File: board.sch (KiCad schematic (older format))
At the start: 13 parts, among them J1 chip_inst_mem_o, J10 chip_data_mem_o_1, J11 base, J12 power, J2 chip_data_mem_o_1, J3 data_mem_i, J4 chip_data_mem_o_1, J5 data_mem_i, J6 chip_data_mem_o_3, J7 inst_mem_i, J8 inst_mem_i, J9 chip_data_mem_o_1, U1 BERYL-MBLite

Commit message: Change headers to SMD and add decoupling capacitors
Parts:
- removed J10, J4, J9: chip_data_mem_o_1, Connector_PinSocket_2.54mm:PinSocket_1x16_P2.54mm_Vertical, symbol Connector:Conn_01x16_Female
- removed J5: data_mem_i, Connector_PinSocket_2.54mm:PinSocket_1x17_P2.54mm_Vertical, symbol Connector:Conn_01x17_Female
- removed J6: chip_data_mem_o_3, Connector_PinSocket_2.54mm:PinSocket_1x06_P2.54mm_Vertical, symbol Connector:Conn_01x06_Female
- removed J8: inst_mem_i, Connector_PinSocket_2.54mm:PinSocket_1x16_P2.54mm_Vertical, symbol Connector:Conn_01x16_Female
- added C1, C10, C11, C12, C13, C14, C15, C16, C17, C18, C19, C2, C20, C21, C22, C23, C24, C25, C3, C4, C5, C6, C7, C8, C9: 100n, Capacitor_SMD:C_0805_2012Metric_Pad1.15x1.40mm_HandSolder, symbol Device:C_Small
- added H1, H2, H3, H4: MountingHole, MountingHole:MountingHole_2.5mm, symbol Mechanical:MountingHole
- added J4: chip_data_mem_o_1, Connector_PinSocket_2.54mm:PinSocket_2x18_P2.54mm_Vertical_SMD, symbol Connector:Conn_01x35_Female
- J1: footprint Connector_PinSocket_2.54mm:PinSocket_1x17_P2.54mm_Vertical -> Connector_PinSocket_2.54mm:PinSocket_2x09_P2.54mm_Vertical_SMD
- J11: footprint Connector_PinSocket_2.54mm:PinSocket_1x05_P2.54mm_Vertical -> Connector_PinSocket_2.54mm:PinSocket_2x03_P2.54mm_Vertical_SMD; symbol Connector:Conn_01x05_Female -> Connector:Conn_01x06_Female
- J12: footprint Connector_PinSocket_2.54mm:PinSocket_1x08_P2.54mm_Vertical -> Connector_PinSocket_2.54mm:PinSocket_2x04_P2.54mm_Vertical_SMD
- J2: footprint Connector_PinSocket_2.54mm:PinSocket_1x16_P2.54mm_Vertical -> Connector_PinSocket_2.54mm:PinSocket_2x18_P2.54mm_Vertical_SMD; symbol Connector:Conn_01x16_Female -> Connector:Conn_01x35_Female
- J3: footprint Connector_PinSocket_2.54mm:PinSocket_1x16_P2.54mm_Vertical -> Connector_PinSocket_2.54mm:PinSocket_2x17_P2.54mm_Vertical_SMD; symbol Connector:Conn_01x16_Female -> Connector:Conn_01x34_Female
- J7: footprint Connector_PinSocket_2.54mm:PinSocket_1x16_P2.54mm_Vertical -> Connector_PinSocket_2.54mm:PinSocket_2x16_P2.54mm_Vertical_SMD; symbol Connector:Conn_01x16_Female -> Connector:Conn_01x32_Female
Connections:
- net +1V8: now also C11.1, C12.1, C13.1, C14.1, C15.1, C16.1, C17.1, C18.1, C19.1, C20.1, C21.1, C22.1, C23.1, C24.1, C25.1
- net +3V3: now also C1.1, C10.1, C2.1, C3.1, C4.1, C5.1, C6.1, C7.1, C8.1, C9.1
- net GND: now also J11.6 (Pin_6), C1.2, C10.2, C11.2, C12.2, C13.2, C14.2, C15.2, C16.2, C17.2, C18.2, C19.2, C2.2, C20.2, C21.2, C22.2, C23.2, C24.2, C25.2, C3.2, C4.2, C5.2, C6.2, C7.2, C8.2, C9.2
- net at U1.153 (data_mem_i_32): now also J3.33 (Pin_33)
- net at U1.154 (data_mem_i_31): now also J3.32 (Pin_32)
- net at U1.155 (data_mem_i_30): now also J3.31 (Pin_31)
- net at U1.156 (data_mem_i_29): now also J3.30 (Pin_30)
- net at U1.157 (data_mem_i_28): now also J3.29 (Pin_29)
- net at U1.158 (data_mem_i_27): now also J3.28 (Pin_28)
- net at U1.159 (data_mem_i_26): now also J3.27 (Pin_27)
- net at U1.160 (data_mem_i_25): now also J3.26 (Pin_26)
- net at U1.163 (data_mem_i_24): now also J3.25 (Pin_25)
- net at U1.164 (data_mem_i_23): now also J3.24 (Pin_24)
- net at U1.165 (data_mem_i_22): now also J3.23 (Pin_23)
- net at U1.166 (data_mem_i_21): now also J3.22 (Pin_22)
- net at U1.167 (data_mem_i_20): now also J3.21 (Pin_21)
- net at U1.168 (data_mem_i_19): now also J3.20 (Pin_20)
- net at U1.169 (data_mem_i_18): now also J3.19 (Pin_19)
- net at U1.170 (data_mem_i_17): now also J3.18 (Pin_18)
- net at U1.171 (data_mem_i_16): now also J3.17 (Pin_17)
- net at U1.1 (inst_mem_i_22): now also J7.10 (Pin_10)
- net at U1.10 (inst_mem_i_15): now also J7.17 (Pin_17); no longer J7.1 (Pin_1)
- net at U1.11 (inst_mem_i_14): now also J7.18 (Pin_18); no longer J7.2 (Pin_2)
- net at U1.12 (inst_mem_i_13): now also J7.19 (Pin_19); no longer J7.3 (Pin_3)
- net at U1.13 (inst_mem_i_12): now also J7.20 (Pin_20); no longer J7.4 (Pin_4)
- net at U1.14 (inst_mem_i_11): now also J7.21 (Pin_21); no longer J7.5 (Pin_5)
- net at U1.15 (inst_mem_i_10): now also J7.22 (Pin_22); no longer J7.6 (Pin_6)
- net at U1.18 (inst_mem_i_9): now also J7.23 (Pin_23); no longer J7.7 (Pin_7)
- net at U1.19 (inst_mem_i_8): now also J7.24 (Pin_24); no longer J7.8 (Pin_8)
- net at U1.192 (inst_mem_i_31): now also J7.1 (Pin_1)
- net at U1.193 (inst_mem_i_30): now also J7.2 (Pin_2)
- net at U1.2 (inst_mem_i_21): now also J7.11 (Pin_11)
- net at U1.20 (inst_mem_i_7): now also J7.25 (Pin_25); no longer J7.9 (Pin_9)
- net at U1.202 (inst_mem_i_29): now also J7.3 (Pin_3)
- net at U1.203 (inst_mem_i_28): now also J7.4 (Pin_4)
- net at U1.204 (inst_mem_i_27): now also J7.5 (Pin_5)
- net at U1.205 (inst_mem_i_26): now also J7.6 (Pin_6)
- net at U1.206 (inst_mem_i_25): now also J7.7 (Pin_7)
- net at U1.207 (inst_mem_i_24): now also J7.8 (Pin_8)
- net at U1.208 (inst_mem_i_23): now also J7.9 (Pin_9)
- net at U1.21 (inst_mem_i_6): now also J7.26 (Pin_26); no longer J7.10 (Pin_10)
- net at U1.22 (inst_mem_i_5): now also J7.27 (Pin_27); no longer J7.11 (Pin_11)
- net at U1.23 (inst_mem_i_4): now also J7.28 (Pin_28); no longer J7.12 (Pin_12)
- net at U1.24 (inst_mem_i_3): now also J7.29 (Pin_29); no longer J7.13 (Pin_13)
- net at U1.27 (inst_mem_i_2): now also J7.30 (Pin_30); no longer J7.14 (Pin_14)
- net at U1.28 (inst_mem_i_1): now also J7.31 (Pin_31); no longer J7.15 (Pin_15)
- net at U1.29 (inst_mem_i_0): now also J7.32 (Pin_32); no longer J7.16 (Pin_16)
- net at U1.3 (inst_mem_i_20): now also J7.12 (Pin_12)
- net at U1.4 (inst_mem_i_19): now also J7.13 (Pin_13)
- net at U1.5 (inst_mem_i_18): now also J7.14 (Pin_14)
- net at U1.6 (inst_mem_i_17): now also J7.15 (Pin_15)
- net at U1.7 (inst_mem_i_16): now also J7.16 (Pin_16)
- net at U1.100 (chip_data_mem_o_20): now also J2.21 (Pin_21)
- net at U1.101 (chip_data_mem_o_19): now also J2.20 (Pin_20)
- net at U1.102 (chip_data_mem_o_18): now also J2.19 (Pin_19)
- net at U1.103 (chip_data_mem_o_17): now also J2.18 (Pin_18)
- net at U1.104 (chip_data_mem_o_16): now also J2.17 (Pin_17)
- net at U1.107 (chip_data_mem_o_36): now also J4.2 (Pin_2)
- net at U1.108 (chip_data_mem_o_37): now also J4.3 (Pin_3)
- net at U1.109 (chip_data_mem_o_38): now also J4.4 (Pin_4)
- net at U1.110 (chip_data_mem_o_39): now also J4.5 (Pin_5)
- net at U1.111 (chip_data_mem_o_40): now also J4.6 (Pin_6)
- net at U1.112 (chip_data_mem_o_41): now also J4.7 (Pin_7)
- net at U1.113 (chip_data_mem_o_42): now also J4.8 (Pin_8)
- net at U1.114 (chip_data_mem_o_43): now also J4.9 (Pin_9)
- net at U1.115 (chip_data_mem_o_44): now also J4.10 (Pin_10)
- net at U1.118 (chip_data_mem_o_45): now also J4.11 (Pin_11)
- net at U1.119 (chip_data_mem_o_46): now also J4.12 (Pin_12)
- net at U1.122 (chip_data_mem_o_47): now also J4.13 (Pin_13)
- net at U1.123 (chip_data_mem_o_48): now also J4.14 (Pin_14)
- net at U1.124 (chip_data_mem_o_49): now also J4.15 (Pin_15)
- net at U1.125 (chip_data_mem_o_50): now also J4.16 (Pin_16)
- net at U1.126 (chip_data_mem_o_51): now also J4.17 (Pin_17)
- net at U1.127 (chip_data_mem_o_52): now also J4.18 (Pin_18)
- net at U1.128 (chip_data_mem_o_53): now also J4.19 (Pin_19)
- net at U1.129 (chip_data_mem_o_54): now also J4.20 (Pin_20)
- net at U1.130 (chip_data_mem_o_55): now also J4.21 (Pin_21)
- net at U1.131 (chip_data_mem_o_56): now also J4.22 (Pin_22)
- net at U1.132 (chip_data_mem_o_57): now also J4.23 (Pin_23)
- net at U1.133 (chip_data_mem_o_58): now also J4.24 (Pin_24)
- net at U1.136 (chip_data_mem_o_59): now also J4.25 (Pin_25)
- net at U1.139 (chip_data_mem_o_60): now also J4.26 (Pin_26)
- net at U1.140 (chip_data_mem_o_61): now also J4.27 (Pin_27)
- net at U1.141 (chip_data_mem_o_62): now also J4.28 (Pin_28)
- net at U1.142 (chip_data_mem_o_63): now also J4.29 (Pin_29)
- net at U1.143 (chip_data_mem_o_64): now also J4.30 (Pin_30)
- net at U1.144 (chip_data_mem_o_65): now also J4.31 (Pin_31)
- net at U1.145 (chip_data_mem_o_66): now also J4.32 (Pin_32)
- net at U1.146 (chip_data_mem_o_67): now also J4.33 (Pin_33)
- net at U1.147 (chip_data_mem_o_68): now also J4.34 (Pin_34)
- net at U1.148 (chip_data_mem_o_69): now also J4.35 (Pin_35)
- net at U1.79 (chip_data_mem_o_35): now also J4.1 (Pin_1)
- net at U1.80 (chip_data_mem_o_34): now also J2.35 (Pin_35)
- net at U1.81 (chip_data_mem_o_33): now also J2.34 (Pin_34)
- net at U1.82 (chip_data_mem_o_32): now also J2.33 (Pin_33)
- net at U1.83 (chip_data_mem_o_31): now also J2.32 (Pin_32)
- net at U1.84 (chip_data_mem_o_30): now also J2.31 (Pin_31)
- net at U1.85 (chip_data_mem_o_29): now also J2.30 (Pin_30)
- net at U1.88 (chip_data_mem_o_28): now also J2.29 (Pin_29)
- net at U1.89 (chip_data_mem_o_27): now also J2.28 (Pin_28)
- net at U1.90 (chip_data_mem_o_26): now also J2.27 (Pin_27)
- net at U1.93 (chip_data_mem_o_25): now also J2.26 (Pin_26)
- net at U1.94 (chip_data_mem_o_24): now also J2.25 (Pin_25)
- net at U1.95 (chip_data_mem_o_23): now also J2.24 (Pin_24)
- net at U1.96 (chip_data_mem_o_22): now also J2.23 (Pin_23)
- net at U1.99 (chip_data_mem_o_21): now also J2.22 (Pin_22)
- no-connect marks 0 -> 1
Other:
- moved on the sheet: J12, U1F

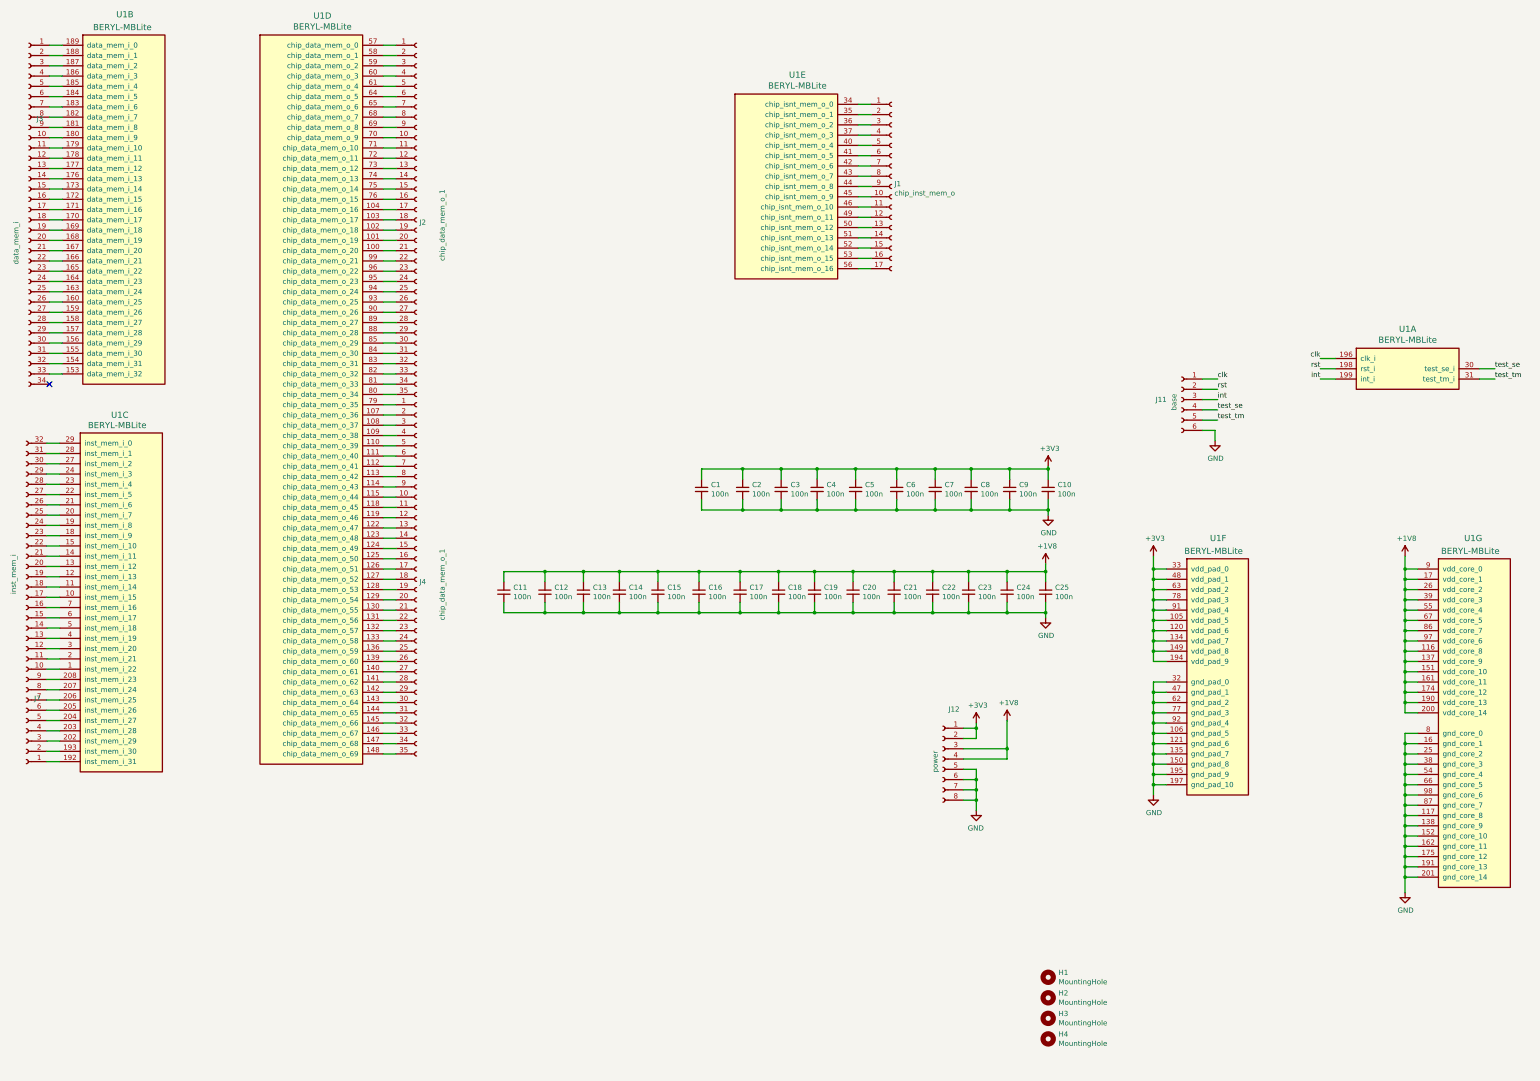
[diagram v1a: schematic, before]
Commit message: Improve capacitors placement
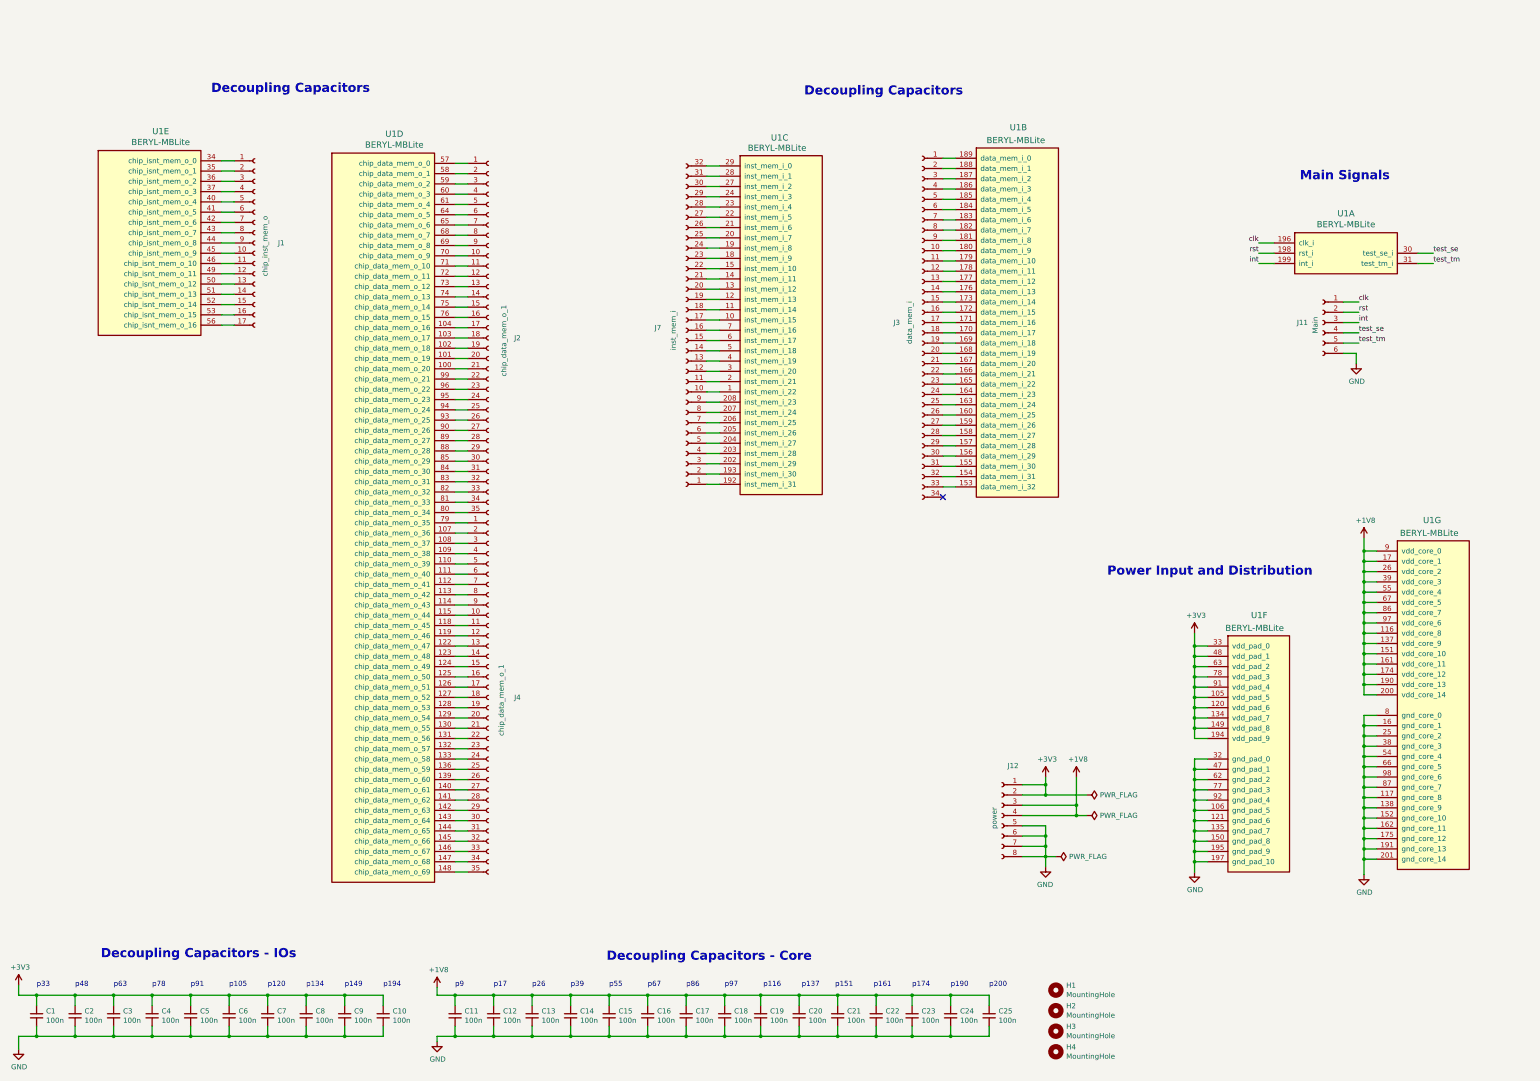
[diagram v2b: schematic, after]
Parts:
- J11: value base -> Main
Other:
- note added: "Decoupling Capacitors"
- note added: "Decoupling Capacitors - Core"
- note added: "Decoupling Capacitors - IOs"
- note added: "Main Signals"
- note added: "Power Input and Distribution"
- note added: "p105"
- note added: "p116"
- note added: "p120"
- note added: "p134"
- note added: "p137"
- note added: "p149"
- note added: "p151"
- note added: "p161"
- note added: "p17"
- note added: "p174"
- note added: "p190"
- note added: "p194"
- note added: "p200"
- note added: "p26"
- note added: "p33"
- note added: "p39"
- note added: "p48"
- note added: "p55"
- note added: "p63"
- note added: "p67"
- note added: "p78"
- note added: "p86"
- note added: "p9"
- note added: "p91"
- note added: "p97"
- moved on the sheet: C1, C10, C11, C12, C13, C14, C15, C16, C17, C18, C19, C2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
